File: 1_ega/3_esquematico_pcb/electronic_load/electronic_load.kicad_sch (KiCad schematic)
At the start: 47 parts, among them J1 Encoder, J10 5V, J11 LOAD, J14 INA219, J15 VCC, J16 LCD_I2C, J17 EGB_I2C, J18 EGB_UART, J2 RTC_I2C, J3 GND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

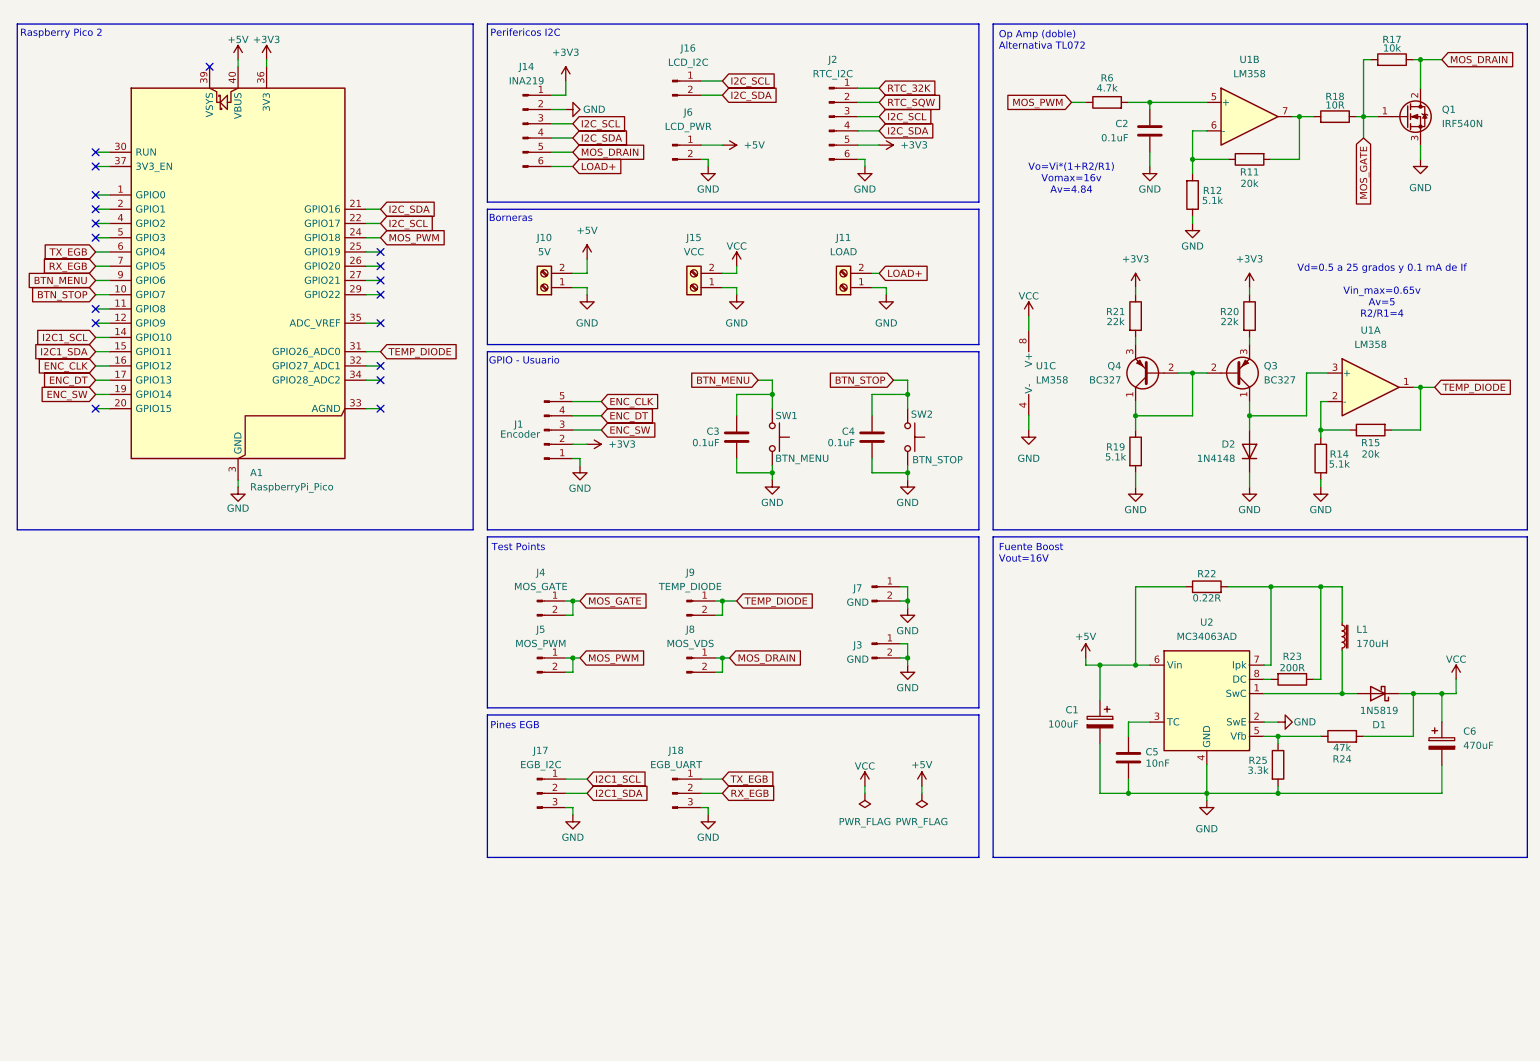
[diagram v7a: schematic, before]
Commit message: feat: add sd card module pins and leds
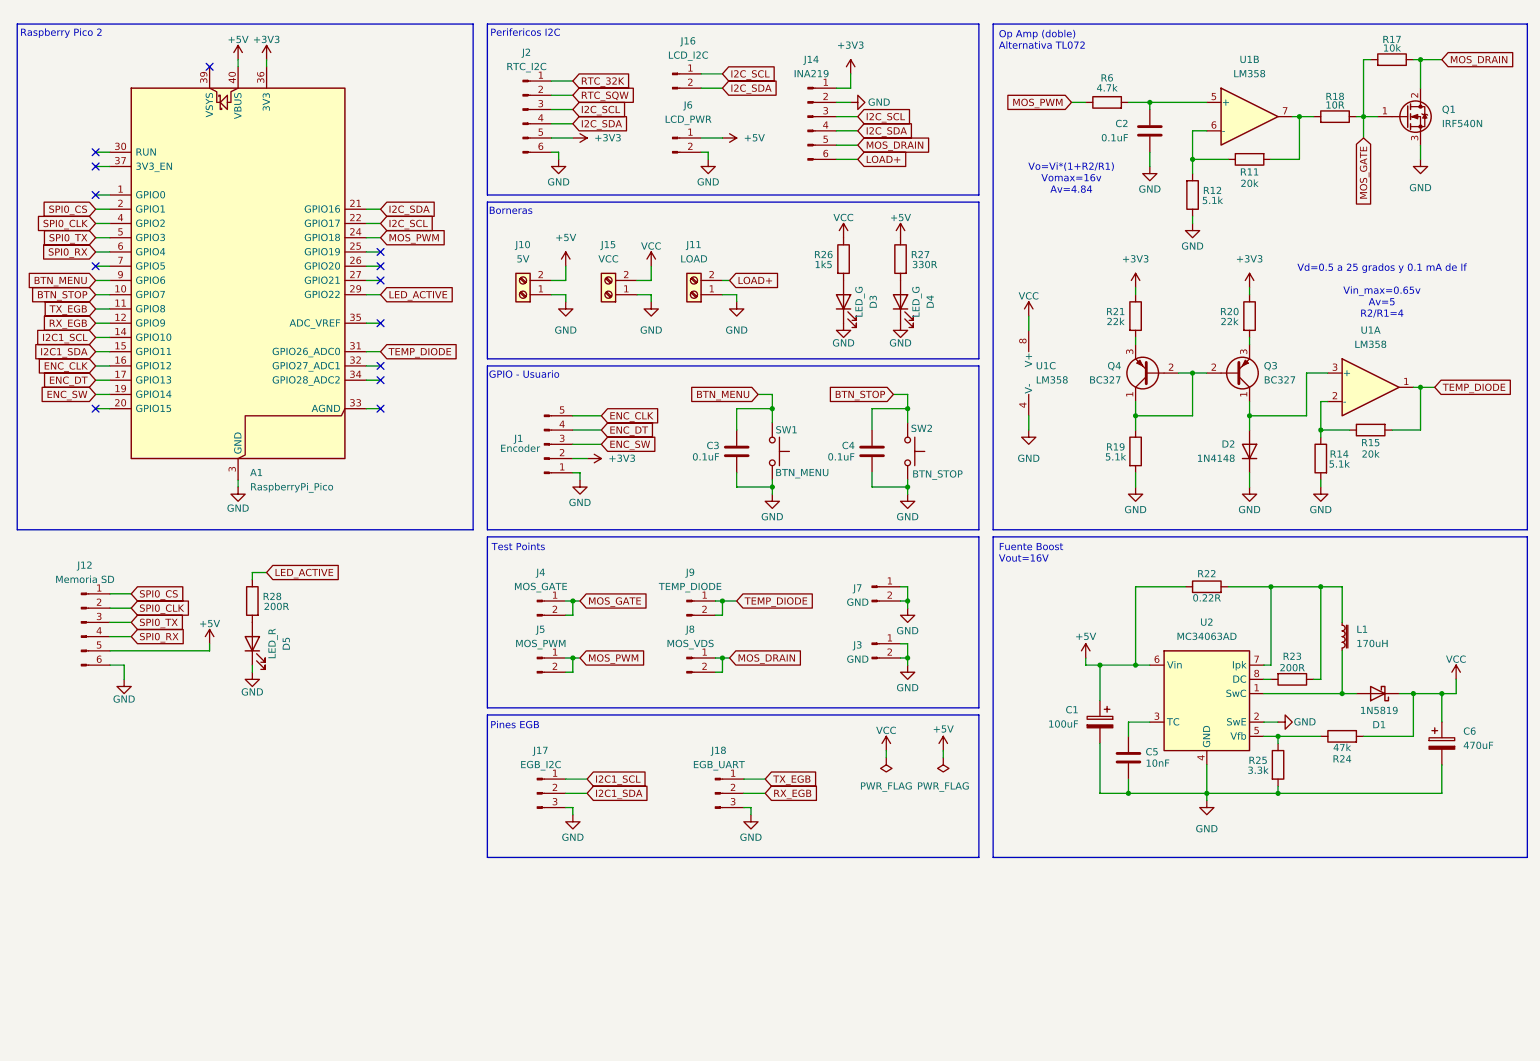
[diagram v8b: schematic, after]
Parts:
- added D3, D4: LED_G, LED_THT:LED_D3.0mm, symbol Device:LED
- added D5: LED_R, LED_THT:LED_D3.0mm, symbol Device:LED
- added J12: Memoria SD, Connector_PinSocket_2.54mm:PinSocket_1x06_P2.54mm_Vertical, symbol Connector:Conn_01x06_Pin
- added R26: 1k5, Resistor_THT:R_Axial_DIN0207_L6.3mm_D2.5mm_P10.16mm_Horizontal, symbol Device:R
- added R27: 330R, Resistor_THT:R_Axial_DIN0207_L6.3mm_D2.5mm_P10.16mm_Horizontal, symbol Device:R
- added R28: 200R, Resistor_THT:R_Axial_DIN0207_L6.3mm_D2.5mm_P10.16mm_Horizontal, symbol Device:R
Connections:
- net +5V: now also J12.5 (Pin_5), R27.1
- net GND: now also D3.1 (K), D4.1 (K), D5.1 (K), J12.6 (Pin_6)
- net RX_EGB: now also A1.12 (GPIO9); no longer A1.7 (GPIO5)
- net TX_EGB: now also A1.11 (GPIO8); no longer A1.6 (GPIO4)
- net VCC: now also R26.1
- net SPI0_CS: now reaches A1.2 (GPIO1)
- net SPI0_CS: now also J12.1 (Pin_1)
- net LED_ACTIVE: now reaches A1.29 (GPIO22)
- net LED_ACTIVE: now also R28.1
- net SPI0_CLK: now reaches A1.4 (GPIO2)
- net SPI0_CLK: now also J12.2 (Pin_2)
- net SPI0_TX: now reaches A1.5 (GPIO3)
- net SPI0_TX: now also J12.3 (Pin_3)
- new net: D3.2 (A), R26.2
- new net: D4.2 (A), R27.2
- new net: D5.2 (A), R28.2
- new net SPI0_RX: A1.6 (GPIO4), J12.4 (Pin_4)
- no-connect marks 18 -> 13
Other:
- moved on the sheet: C3, C4, J1, J10, J11, J14, J15, J16, J18, J2, J6, SW1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
